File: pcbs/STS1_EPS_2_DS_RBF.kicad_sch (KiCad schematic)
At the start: 33 parts, among them Q1 2N7002, Q10 2N7002, Q11 2N7002, Q14 2N7002, Q15 2N7002, Q18 2N7002, Q19 2N7002, Q20 2N7002, Q7 2N7002

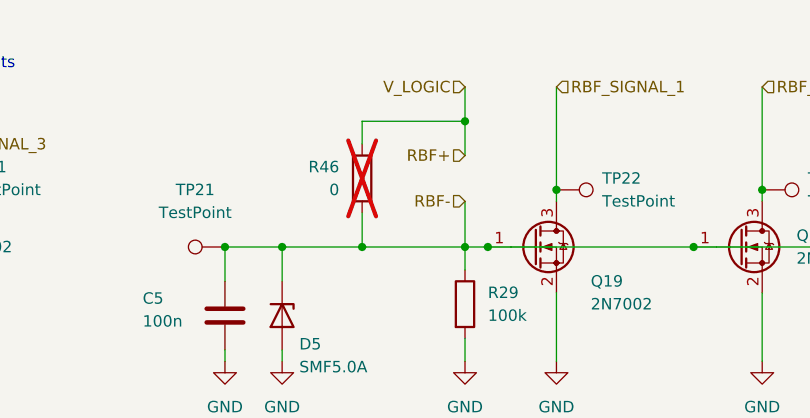
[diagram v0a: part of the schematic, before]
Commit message: Added resistor for the RBF pin.
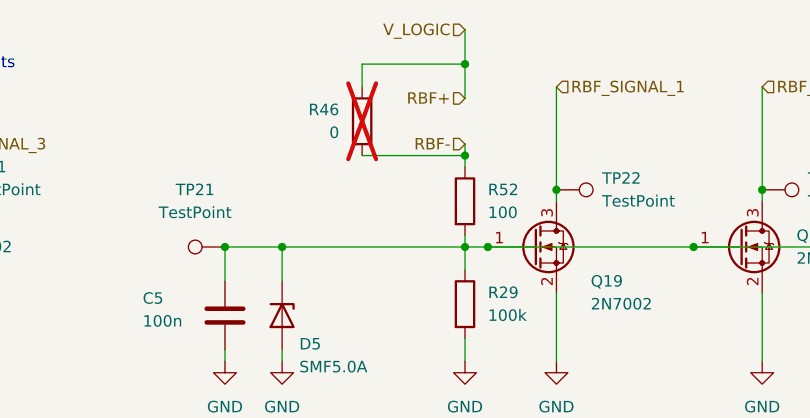
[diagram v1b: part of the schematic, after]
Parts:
- added R52: 100, Resistor_SMD:R_0805_2012Metric, symbol Device:R
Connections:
- net RBF-: now also R52.1; no longer C5.1, D5.1 (K), Q1.1 (G), Q19.1 (G), Q20.1 (G), R29.1, TP21.1
- new net: C5.1, D5.1 (K), Q1.1 (G), Q19.1 (G), Q20.1 (G), R29.1, R52.2, TP21.1
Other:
- moved on the sheet: R46
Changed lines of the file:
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@@
 	)
 	(junction
-		(at 137.16 40.64)
-		(diameter 0)
-		(color 0 0 0 0)
-	)
-	(junction
 		(at 173.99 40.64)
 		(diameter 0)
@@
 	)
 	(junction
+		(at 148.59 30.48)
+		(diameter 0)
+		(color 0 0 0 0)
+	)
+	(junction
 		(at 87.63 33.02)
 		(diameter 0)
@@
 	)
 	(junction
-		(at 148.59 26.67)
+		(at 148.59 20.32)
 		(diameter 0)
 		(color 0 0 0 0)
@@
 	(wire
 		(pts
-			(xy 148.59 22.86) (xy 148.59 26.67)
+			(xy 148.59 16.51) (xy 148.59 20.32)
 		)
 		(stroke
@@
 	(wire
 		(pts
+			(xy 137.16 30.48) (xy 148.59 30.48)
+		)
+		(stroke
+			(width 0)
+			(type default)
+		)
+	)
+	(wire
+		(pts
 			(xy 35.56 78.74) (xy 38.1 78.74)
 		)
@@
 	(wire
 		(pts
-			(xy 148.59 26.67) (xy 148.59 30.48)
+			(xy 148.59 20.32) (xy 148.59 24.13)
 		)
 		(stroke
@@
 	(wire
 		(pts
-			(xy 137.16 40.64) (xy 148.59 40.64)
+			(xy 64.77 33.02) (xy 64.77 34.29)
 		)
 		(stroke
@@
 	(wire
 		(pts
-			(xy 64.77 33.02) (xy 64.77 34.29)
+			(xy 64.77 83.82) (xy 64.77 91.44)
 		)
 		(stroke
@@
 	(wire
 		(pts
-			(xy 64.77 83.82) (xy 64.77 91.44)
+			(xy 35.56 49.53) (xy 35.56 52.07)
 		)
 		(stroke
@@
 	(wire
 		(pts
-			(xy 35.56 49.53) (xy 35.56 52.07)
+			(xy 148.59 29.21) (xy 148.59 30.48)
 		)
 		(stroke
@@
 	(wire
 		(pts
-			(xy 148.59 35.56) (xy 148.59 40.64)
+			(xy 45.72 44.45) (xy 45.72 52.07)
 		)
 		(stroke
@@
 	(wire
 		(pts
-			(xy 45.72 44.45) (xy 45.72 52.07)
+			(xy 148.59 30.48) (xy 148.59 31.75)
 		)
 		(stroke
@@
 	(wire
 		(pts
-			(xy 128.27 40.64) (xy 137.16 40.64)
+			(xy 128.27 40.64) (xy 148.59 40.64)
 		)
 		(stroke
@@
 	(wire
 		(pts
-			(xy 148.59 26.67) (xy 137.16 26.67)
+			(xy 148.59 20.32) (xy 137.16 20.32)
 		)
 		(stroke
@@
 	(wire
 		(pts
-			(xy 137.16 26.67) (xy 137.16 29.21)
+			(xy 137.16 20.32) (xy 137.16 22.86)
 		)
 		(stroke
@@
 	(wire
 		(pts
+			(xy 148.59 39.37) (xy 148.59 40.64)
+		)
+		(stroke
+			(width 0)
+			(type default)
+		)
+	)
+	(wire
+		(pts
 			(xy 45.72 33.02) (xy 45.72 34.29)
 		)
@@
 		)
 	)
-	(wire
-		(pts
-			(xy 137.16 36.83) (xy 137.16 40.64)
-		)
-		(stroke
-			(width 0)
-			(type default)
-		)
-	)
 	(text "Open drain outputs"
 		(exclude_from_sim no)
@@
 	(hierarchical_label "RBF+"
 		(shape input)
-		(at 148.59 30.48 180)
+		(at 148.59 24.13 180)
 		(fields_autoplaced yes)
 		(effects
@@
 	(hierarchical_label "RBF-"
 		(shape input)
-		(at 148.59 35.56 180)
+		(at 148.59 29.21 180)
 		(fields_autoplaced yes)
 		(effects
@@
 	(hierarchical_label "V_LOGIC"
 		(shape input)
-		(at 148.59 22.86 180)
+		(at 148.59 16.51 180)
 		(fields_autoplaced yes)
 		(effects
@@
 	)
 	(symbol
+		(lib_id "Device:R")
+		(at 148.59 35.56 0)
+		(unit 1)
+		(exclude_from_sim no)
+		(in_bom yes)
+		(on_board yes)
+		(dnp no)
+		(fields_autoplaced yes)
+		(property "Reference" "R52"
+			(at 151.13 34.2899 0)
+			(effects
+				(font
+					(size 1.27 1.27)
+				)
+				(justify left)
+			)
+		)
+		(property "Value" "100"
+			(at 151.13 36.8299 0)
+			(effects
+				(font
+					(size 1.27 1.27)
+				)
+				(justify left)
+			)
+		)
+		(property "Footprint" "Resistor_SMD:R_0805_2012Metric"
+			(at 146.812 35.56 90)
+			(effects
+				(font
+					(size 1.27 1.27)
+				)
+				(hide yes)
+			)
+		)
+		(property "Datasheet" "~"
+			(at 148.59 35.56 0)
+			(effects
+				(font
+					(size 1.27 1.27)
+				)
+				(hide yes)
+			)
+		)
+		(property "Description" ""
+			(at 148.59 35.56 0)
+			(effects
+				(font
+					(size 1.27 1.27)
+				)
+				(hide yes)
+			)
+		)
+		(property "Part Nr." "TNPW0805100KFEEA"
+			(at 148.59 22.86 0)
+			(effects
+				(font
+					(size 1.27 1.27)
+				)
+				(hide yes)
+			)
+		)
+		(pin "1"
+		)
+		(pin "2"
+		)
+		(instances
+			(project "STS1_EPS_2"
+				(path "/38c03ff7-ea47-4d00-b37d-ddcaa7d87722/782ccd28-d43b-446c-892c-2705ffe9f1f3"
+					(reference "R52")
+					(unit 1)
+				)
+			)
+		)
+	)
+	(symbol
 		(lib_id "Transistor_FET:2N7002")
 		(at 156.21 40.64 0)
@@
 	(symbol
 		(lib_id "Device:R")
-		(at 137.16 33.02 0)
+		(at 137.16 26.67 0)
 		(mirror x)
 		(unit 1)
@@
 		(dnp yes)
 		(property "Reference" "R46"
-			(at 134.62 31.7499 0)
+			(at 134.62 25.3999 0)
 			(effects
 				(font
@@
 		)
 		(property "Value" "0"
-			(at 134.62 34.2899 0)
+			(at 134.62 27.9399 0)
 			(effects
 				(font
@@
 		)
 		(property "Footprint" "Resistor_SMD:R_0805_2012Metric"
-			(at 135.382 33.02 90)
+			(at 135.382 26.67 90)
 			(effects
 				(font
@@
 		)
 		(property "Datasheet" "~"
-			(at 137.16 33.02 0)
+			(at 137.16 26.67 0)
 			(effects
 				(font
@@
 		)
 		(property "Description" ""
-			(at 137.16 33.02 0)
+			(at 137.16 26.67 0)
 			(effects
 				(font
@@
 		)
 		(property "Part Nr." ""
-			(at 148.59 46.99 0)
+			(at 148.59 40.64 0)
 			(effects
 				(font

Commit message: Updated a few inconsistent part numbers.
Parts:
- R52: Part Nr. TNPW0805100KFEEA -> TNPW0805100RFETA
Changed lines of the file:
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@@
 			)
 		)
-		(property "Part Nr." "TNPW0805100KFEEA"
+		(property "Part Nr." "TNPW0805100RFETA"
 			(at 148.59 22.86 0)
 			(effects
